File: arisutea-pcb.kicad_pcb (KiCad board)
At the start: 2 copper layers, 339.1 x 121 mm, 179 parts, among them J10 PF6, J11 PF7, J12 VCC, J13 D+, J14 D-, J15 GND, J2 MISO, J3 VCC, J4 SCK, J5 MOSI, J6 RES, J7 GND, J8 PF4, J9 PF5, SW1 SW_Push, SW10 SW_Push, SW11 SW_Push, SW12 SW_Push, SW13 SW_Push, SW14 SW_Push, SW15 SW_Push, SW16 SW_Push, SW17 SW_Push, SW18 SW_Push, SW19 SW_Push, SW2 SW_Push, SW20 SW_Push, SW21 SW_Push, SW22 SW_Push, SW23 SW_Push, SW24 SW_Push, SW25 SW_Push, SW26 SW_Push, SW27 SW_Push, SW28 SW_Push, SW29 SW_Push, SW3 SW_Push, SW30 SW_Push, SW31 SW_Push, SW32 SW_Push, SW33 SW_Push, SW34 SW_Push, SW35 SW_Push, SW36 SW_Push, SW37 SW_Push, SW38 SW_Push, SW39 SW_Push, SW4 SW_Push, SW40 SW_Push, SW41 SW_Push, SW42 SW_Push, SW43 SW_Push, SW44 SW_Push, SW45 SW_Push, SW46 SW_Push, SW47 SW_Push, SW48 SW_Push, SW49 SW_Push, SW5 SW_Push, SW50 SW_Push, SW51 SW_Push, SW52 SW_Push, SW53 SW_Push, SW54 SW_Push, SW55 SW_Push, SW56 SW_Push, SW57 SW_Push, SW58 SW_Push, SW59 SW_Push, SW6 SW_Push, SW60 SW_Push, SW61 SW_Push, SW62 SW_Push, SW63 SW_Push, SW64 SW_Push, SW65 SW_Push, SW66 SW_Push, SW7 SW_Push, SW8 SW_Push, SW9 SW_Push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

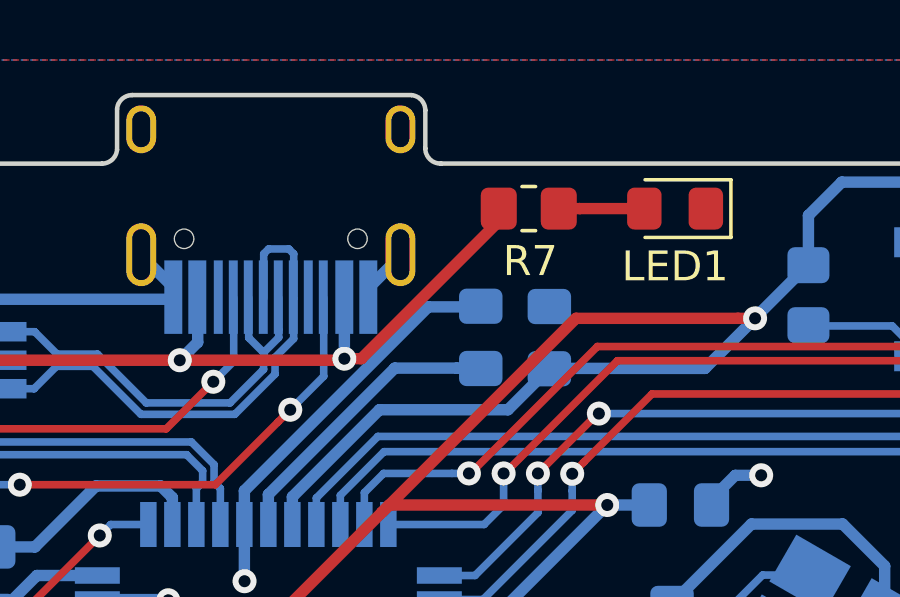
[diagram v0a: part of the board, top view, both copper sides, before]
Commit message: update photos
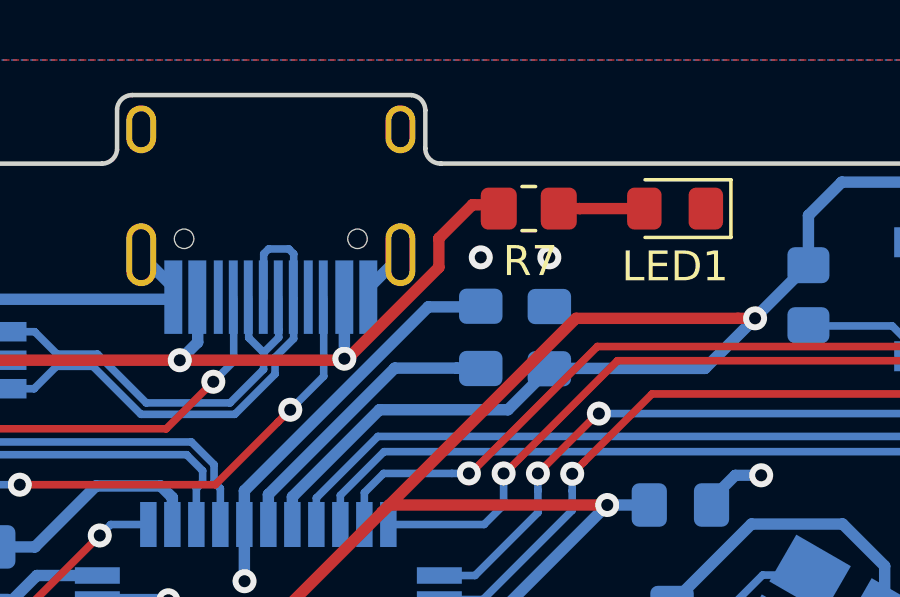
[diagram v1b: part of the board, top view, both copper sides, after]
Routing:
- net GND: vias 11 -> 13
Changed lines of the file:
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@@
     (thickness 1.6)
     (drawings 1392)
-    (tracks 1044)
+    (tracks 1048)
     (zones 0)
     (modules 179)
@@
   (segment (start 171.558001 44.849999) (end 171.958 44.45) (width 0.381) (layer B.Cu) (net 2))
   (segment (start 171.044 45.364) (end 171.558001 44.849999) (width 0.381) (layer B.Cu) (net 2))
+  (via (at 184.785 27.559) (size 0.8) (drill 0.4) (layers F.Cu B.Cu) (net 2))
+  (via (at 182.499 27.559) (size 0.8) (drill 0.4) (layers F.Cu B.Cu) (net 2))
   (segment (start 191.894328 38.149572) (end 193.451863 38.149572) (width 0.254) (layer B.Cu) (net 3))
   (segment (start 188.8744 41.1695) (end 191.894328 38.149572) (width 0.254) (layer B.Cu) (net 3))
@@
   (segment (start 172.466004 30.988) (end 177.901602 30.988) (width 0.381) (layer F.Cu) (net 4))
   (segment (start 177.901602 30.988) (end 177.952402 30.9372) (width 0.381) (layer F.Cu) (net 4))
-  (segment (start 183.0742 26.381087) (end 183.0742 25.8064) (width 0.381) (layer F.Cu) (net 4))
-  (segment (start 178.518087 30.9372) (end 183.0742 26.381087) (width 0.381) (layer F.Cu) (net 4))
-  (segment (start 177.952402 30.9372) (end 178.518087 30.9372) (width 0.381) (layer F.Cu) (net 4))
+  (segment (start 182.2196 25.8064) (end 183.0742 25.8064) (width 0.381) (layer F.Cu) (net 4))
+  (segment (start 181.102 26.924) (end 182.2196 25.8064) (width 0.381) (layer F.Cu) (net 4))
+  (segment (start 181.102 27.894133) (end 181.102 26.924) (width 0.381) (layer F.Cu) (net 4))
+  (segment (start 177.952402 30.9372) (end 178.058933 30.9372) (width 0.381) (layer F.Cu) (net 4))
+  (segment (start 178.058933 30.9372) (end 181.102 27.894133) (width 0.381) (layer F.Cu) (net 4))
   (segment (start 181.699 31.251) (end 182.499 31.251) (width 0.381) (layer B.Cu) (net 5))
   (segment (start 179.63175 31.251) (end 181.699 31.251) (width 0.381) (layer B.Cu) (net 5))
@@
   (segment (start 175.764 30.23) (end 175.764 29.972) (width 0.254) (layer B.Cu) (net 105))
   (segment (start 175.26 30.734) (end 175.764 30.23) (width 0.254) (layer B.Cu) (net 105))
-  (segment (start 167.6298 30.038) (end 166.577 30.038) (width 0.254) (layer B.Cu) (net 105) (status 1000000))
-  (segment (start 175.26 30.6832) (end 175.26 31.2928) (width 0.254) (layer B.Cu) (net 105) (status 1000000))
-  (segment (start 175.26 31.2928) (end 174.1424 32.4104) (width 0.254) (layer B.Cu) (net 105) (status 1000000))
-  (segment (start 174.1424 32.4104) (end 171.3484 32.4104) (width 0.254) (layer B.Cu) (net 105) (status 1000000))
-  (segment (start 168.3766 30.7848) (end 167.6298 30.038) (width 0.254) (layer B.Cu) (net 105) (status 1000000))
-  (segment (start 171.3484 32.4104) (end 169.7228 30.7848) (width 0.254) (layer B.Cu) (net 105) (status 1000000))
-  (segment (start 169.7228 30.7848) (end 168.3766 30.7848) (width 0.254) (layer B.Cu) (net 105) (status 1000000))
+  (segment (start 167.6298 30.038) (end 166.577 30.038) (width 0.254) (layer B.Cu) (net 105))
+  (segment (start 175.26 30.6832) (end 175.26 31.2928) (width 0.254) (layer B.Cu) (net 105))
+  (segment (start 175.26 31.2928) (end 174.1424 32.4104) (width 0.254) (layer B.Cu) (net 105))
+  (segment (start 174.1424 32.4104) (end 171.3484 32.4104) (width 0.254) (layer B.Cu) (net 105))
+  (segment (start 168.3766 30.7848) (end 167.6298 30.038) (width 0.254) (layer B.Cu) (net 105))
+  (segment (start 171.3484 32.4104) (end 169.7228 30.7848) (width 0.254) (layer B.Cu) (net 105))
+  (segment (start 169.7228 30.7848) (end 168.3766 30.7848) (width 0.254) (layer B.Cu) (net 105))
   (via (at 157.48 26.289) (size 0.8) (drill 0.4) (layers F.Cu B.Cu) (net 109))
   (via (at 171.577 46.101) (size 0.8) (drill 0.4) (layers F.Cu B.Cu) (net 109))

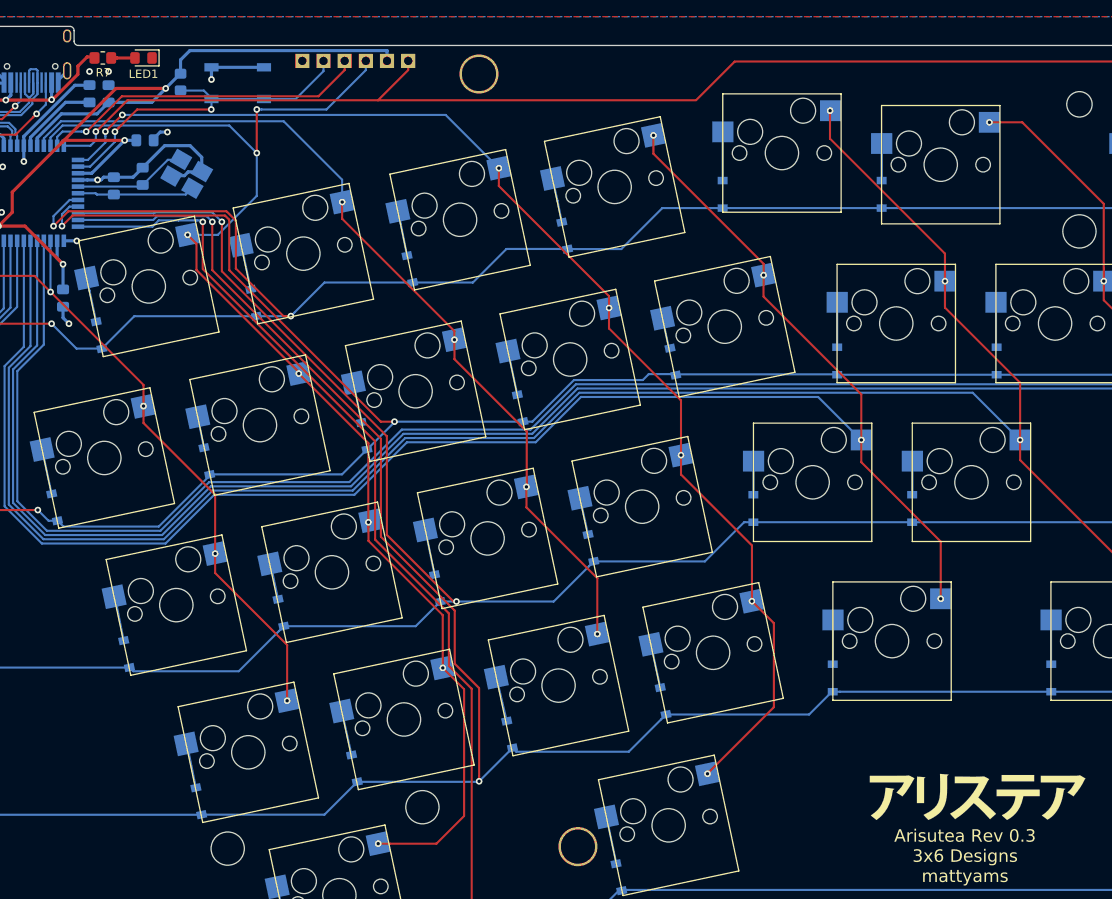
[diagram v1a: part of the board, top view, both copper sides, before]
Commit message: versioning to 0.4
remove LED...../sigh
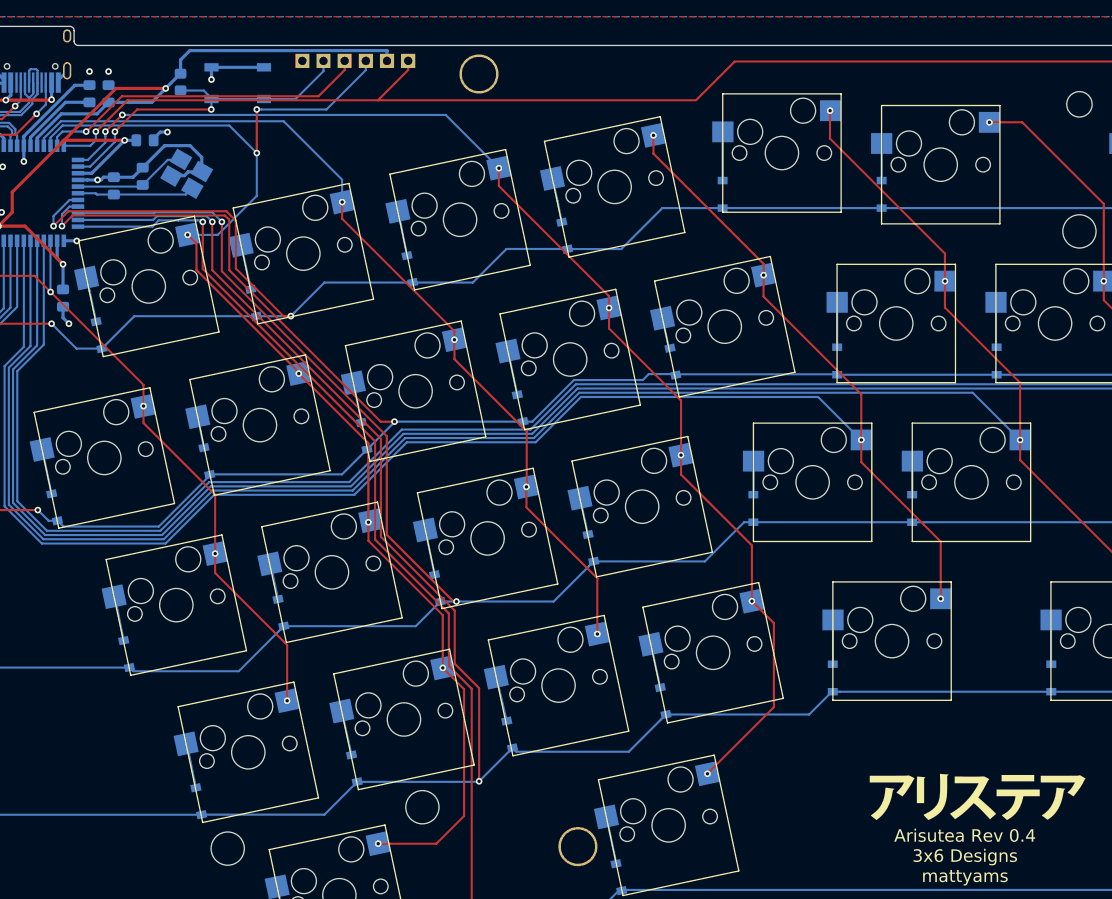
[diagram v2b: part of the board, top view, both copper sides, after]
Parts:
- removed LED1: LED, LED_SMD:LED_0805_2012Metric_Pad1.15x1.40mm_HandSolder
- removed R7: 1K, Resistor_SMD:R_0805_2012Metric_Pad1.20x1.40mm_HandSolder
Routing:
- net VCC: track 44.2 -> 36.4 mm
- net Net-(D67-Pad2): track 2.85 -> 0.00 mm
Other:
- board text added: "Arisutea Rev 0.4 3x6 Designs mattyams"
- board text removed: "Arisutea Rev 0.3 3x6 Designs mattyams"
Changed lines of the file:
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@@
     (thickness 1.6)
     (drawings 1392)
-    (tracks 1048)
+    (tracks 1041)
     (zones 0)
-    (modules 179)
-    (nets 112)
+    (modules 177)
+    (nets 111)
   )
   (page User 389.992 199.136)
@@
   (net 109 +5V)
   (net 110 "Net-(D63-Pad2)")
-  (net 111 "Net-(D67-Pad2)")
   (net_class Default "This is the default net class."
     (clearance 0.127)
@@
     (add_net "Net-(D65-Pad2)")
     (add_net "Net-(D66-Pad2)")
-    (add_net "Net-(D67-Pad2)")
     (add_net "Net-(D7-Pad2)")
     (add_net "Net-(D8-Pad2)")
@@
     )
   )
-  (module LED_SMD:LED_0805_2012Metric_Pad1.15x1.40mm_HandSolder (layer F.Cu)
-    (at 188.976 25.9334 180)
-    (descr "LED SMD 0805 (2012 Metric), square (rectangular) end terminal, IPC_7351 nominal, (Body size source: https://docs.google.com/spreadsheets/d/1BsfQQcO9C6DZCsRaXUlFlo91Tg2WpOkGARC1WS5S8t0/edit?usp=sharing), generated with kicad-footprint-generator")
-    (tags "LED handsolder")
-    (attr smd)
-    (fp_text reference LED1 (at 0 -1.9304) (layer F.SilkS)
-      (effects (font (size 1 1) (thickness 0.15)))
-    )
-    (fp_text value LED (at 3.81 -0.0508) (layer F.Fab)
-      (effects (font (size 1 1) (thickness 0.15)))
-    )
-    (fp_text user %R (at 0 -1.9304) (layer F.Fab)
-      (effects (font (size 1 1) (thickness 0.15)))
-    )
-    (fp_line (start 1.85 0.95) (end -1.85 0.95) (layer F.CrtYd) (width 0.05))
-    (fp_line (start 1.85 -0.95) (end 1.85 0.95) (layer F.CrtYd) (width 0.05))
-    (fp_line (start -1.85 -0.95) (end 1.85 -0.95) (layer F.CrtYd) (width 0.05))
-    (fp_line (start -1.85 0.95) (end -1.85 -0.95) (layer F.CrtYd) (width 0.05))
-    (fp_line (start -1.86 0.96) (end 1 0.96) (layer F.SilkS) (width 0.12))
-    (fp_line (start -1.86 -0.96) (end -1.86 0.96) (layer F.SilkS) (width 0.12))
-    (fp_line (start 1 -0.96) (end -1.86 -0.96) (layer F.SilkS) (width 0.12))
-    (fp_line (start 1 0.6) (end 1 -0.6) (layer F.Fab) (width 0.1))
-    (fp_line (start -1 0.6) (end 1 0.6) (layer F.Fab) (width 0.1))
-    (fp_line (start -1 -0.3) (end -1 0.6) (layer F.Fab) (width 0.1))
-    (fp_line (start -0.7 -0.6) (end -1 -0.3) (layer F.Fab) (width 0.1))
-    (fp_line (start 1 -0.6) (end -0.7 -0.6) (layer F.Fab) (width 0.1))
-    (pad 2 smd roundrect (at 1.025 0 180) (size 1.15 1.4) (layers F.Cu F.Paste F.Mask) (roundrect_rratio 0.217391)
-      (net 111 "Net-(D67-Pad2)"))
-    (pad 1 smd roundrect (at -1.025 0 180) (size 1.15 1.4) (layers F.Cu F.Paste F.Mask) (roundrect_rratio 0.217391)
-      (net 2 GND))
-    (model ${KISYS3DMOD}/LED_SMD.3dshapes/LED_0805_2012Metric.wrl
-      (at (xyz 0 0 0))
-      (scale (xyz 1 1 1))
-      (rotate (xyz 0 0 0))
-    )
-  )
   (module Package_TO_SOT_SMD:SOT-23-6_Handsoldering (layer B.Cu)
     (at 165.227 30.988 180)
@@
     )
   )
-  (module Resistor_SMD:R_0805_2012Metric_Pad1.20x1.40mm_HandSolder (layer F.Cu)
-    (at 184.0992 25.9334)
-    (descr "Resistor SMD 0805 (2012 Metric), square (rectangular) end terminal, IPC_7351 nominal with elongated pad for handsoldering. (Body size source: IPC-SM-782 page 72, https://www.pcb-3d.com/wordpress/wp-content/uploads/ipc-sm-782a_amendment_1_and_2.pdf), generated with kicad-footprint-generator")
-    (tags "resistor handsolder")
-    (attr smd)
-    (fp_text reference R7 (at 0.0508 1.7526) (layer F.SilkS)
-      (effects (font (size 1 1) (thickness 0.15)))
-    )
-    (fp_text value 1K (at 0.0508 -1.6764) (layer F.Fab)
-      (effects (font (size 1 1) (thickness 0.15)))
-    )
-    (fp_text user %R (at 0 0) (layer F.Fab)
-      (effects (font (size 0.5 0.5) (thickness 0.08)))
-    )
-    (fp_line (start 1.85 0.95) (end -1.85 0.95) (layer F.CrtYd) (width 0.05))
-    (fp_line (start 1.85 -0.95) (end 1.85 0.95) (layer F.CrtYd) (width 0.05))
-    (fp_line (start -1.85 -0.95) (end 1.85 -0.95) (layer F.CrtYd) (width 0.05))
-    (fp_line (start -1.85 0.95) (end -1.85 -0.95) (layer F.CrtYd) (width 0.05))
-    (fp_line (start -0.227064 0.735) (end 0.227064 0.735) (layer F.SilkS) (width 0.12))
-    (fp_line (start -0.227064 -0.735) (end 0.227064 -0.735) (layer F.SilkS) (width 0.12))
-    (fp_line (start 1 0.625) (end -1 0.625) (layer F.Fab) (width 0.1))
-    (fp_line (start 1 -0.625) (end 1 0.625) (layer F.Fab) (width 0.1))
-    (fp_line (start -1 -0.625) (end 1 -0.625) (layer F.Fab) (width 0.1))
-    (fp_line (start -1 0.625) (end -1 -0.625) (layer F.Fab) (width 0.1))
-    (pad 2 smd roundrect (at 1 0) (size 1.2 1.4) (layers F.Cu F.Paste F.Mask) (roundrect_rratio 0.208333)
-      (net 111 "Net-(D67-Pad2)"))
-    (pad 1 smd roundrect (at -1 0) (size 1.2 1.4) (layers F.Cu F.Paste F.Mask) (roundrect_rratio 0.208333)
-      (net 4 VCC))
-    (model ${KISYS3DMOD}/Resistor_SMD.3dshapes/R_0805_2012Metric.wrl
-      (at (xyz 0 0 0))
-      (scale (xyz 1 1 1))
-      (rotate (xyz 0 0 0))
-    )
-  )
   (module Mounting_Keyboard_Stabilizer:THROUGH_HOLE_M2 (layer F.Cu)
     (at 345.449949 110.157503)
@@
     (effects (font (size 1.5 1.5) (thickness 0.3)))
   )
-  (gr_text "Arisutea Rev 0.3\n3x6 Designs\nmattyams" (at 287.528 121.666) (layer F.SilkS)
+  (gr_text "Arisutea Rev 0.4\n3x6 Designs\nmattyams" (at 287.528 121.666) (layer F.SilkS)
     (effects (font (size 1.5 1.5) (thickness 0.3)))
   )
-  (gr_text "Arisutea Rev 0.3\n3x6 Designs\nmattyams" (at 287.401 121.666) (layer B.SilkS)
+  (gr_text "Arisutea Rev 0.4\n3x6 Designs\nmattyams" (at 287.401 121.666) (layer B.SilkS)
     (effects (font (size 1.5 1.5) (thickness 0.3)) (justify mirror))
   )
@@
   (segment (start 172.466004 30.988) (end 177.901602 30.988) (width 0.381) (layer F.Cu) (net 4))
   (segment (start 177.901602 30.988) (end 177.952402 30.9372) (width 0.381) (layer F.Cu) (net 4))
-  (segment (start 182.2196 25.8064) (end 183.0742 25.8064) (width 0.381) (layer F.Cu) (net 4))
-  (segment (start 181.102 26.924) (end 182.2196 25.8064) (width 0.381) (layer F.Cu) (net 4))
-  (segment (start 181.102 27.894133) (end 181.102 26.924) (width 0.381) (layer F.Cu) (net 4))
-  (segment (start 177.952402 30.9372) (end 178.058933 30.9372) (width 0.381) (layer F.Cu) (net 4))
-  (segment (start 178.058933 30.9372) (end 181.102 27.894133) (width 0.381) (layer F.Cu) (net 4))
   (segment (start 181.699 31.251) (end 182.499 31.251) (width 0.381) (layer B.Cu) (net 5))
   (segment (start 179.63175 31.251) (end 181.699 31.251) (width 0.381) (layer B.Cu) (net 5))
@@
   (segment (start 339.5472 31.4182) (end 339.498 31.369) (width 0.25) (layer B.Cu) (net 110))
   (segment (start 339.5472 36.6278) (end 339.5472 31.4182) (width 0.25) (layer B.Cu) (net 110))
-  (segment (start 185.7992 25.9334) (end 187.951 25.9334) (width 0.381) (layer F.Cu) (net 111))
-  (segment (start 185.0992 25.9334) (end 185.7992 25.9334) (width 0.381) (layer F.Cu) (net 111))
   (zone (net 2) (net_name GND) (layer F.Cu) (hatch edge 0.508)
     (connect_pads (clearance 0.508))
